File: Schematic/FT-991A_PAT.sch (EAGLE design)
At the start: 33 parts, among them Q1 PE4259, Q2 MC78L09ABDR2GOSCT, Q5 NCP553, Q7 J310, Q8 5086, X1 IF_IN, X2 SCP_OUT, X3 SDR_OUT

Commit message: Few more enhancements and impedance control
* Larger ground exposed ground pad near at the screw
* Changed pad for RF components to a rounded layout
* Enlarged the RF wire signal, in order to reduce the internal signal
  impedance
* Better component silk screen
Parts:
- C1, C10, C13, C6: device rcl:C-EUC0805 -> aarf:C-0805
- C11, C7: device rcl:C-EUC3216 -> aarf:C-1206
- D1: device diode:DIODE-SOD323-W -> aarf:D-SOD323
- L2, L3: device rcl-modified:L-EU -> aarf:FB-0805
- R10, R2, R3, R4, R5, R6, R7, R8, R9: device rcl:R-US_R3216 -> aarf:R-1206
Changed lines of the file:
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@@
 </classes>
 <parts>
-<part name="C6" library="rcl" library_urn="urn:adsk.eagle:library:334" deviceset="C-EU" device="C0805" package3d_urn="urn:adsk.eagle:package:23617/2" value="1000pF"/>
-<part name="R5" library="rcl" library_urn="urn:adsk.eagle:library:334" deviceset="R-US_" device="R3216" package3d_urn="urn:adsk.eagle:package:23557/2" value="100kΩ"/>
+<part name="C6" library="aarf" deviceset="C-0805" device="" value="1000pF"/>
+<part name="R5" library="aarf" deviceset="R-1206" device="" value="100kΩ"/>
 <part name="Q8" library="aarf" deviceset="2SC5086" device="" value="5086"/>
-<part name="R7" library="rcl" library_urn="urn:adsk.eagle:library:334" deviceset="R-US_" device="R3216" package3d_urn="urn:adsk.eagle:package:23557/2" value="1kΩ"/>
-<part name="C10" library="rcl" library_urn="urn:adsk.eagle:library:334" deviceset="C-EU" device="C0805" package3d_urn="urn:adsk.eagle:package:23617/2" value="1000pF"/>
+<part name="R7" library="aarf" deviceset="R-1206" device="" value="1kΩ"/>
+<part name="C10" library="aarf" deviceset="C-0805" device="" value="1000pF"/>
 <part name="GND11" library="supply1" deviceset="GNDA" device=""/>
-<part name="R6" library="rcl" library_urn="urn:adsk.eagle:library:334" deviceset="R-US_" device="R3216" package3d_urn="urn:adsk.eagle:package:23557/2" value="220Ω"/>
-<part name="C7" library="rcl" library_urn="urn:adsk.eagle:library:334" deviceset="C-EU" device="C3216" package3d_urn="urn:adsk.eagle:package:23628/2" value="0.1µF"/>
+<part name="R6" library="aarf" deviceset="R-1206" device="" value="220Ω"/>
+<part name="C7" library="aarf" deviceset="C-1206" device="" value="0.1µF"/>
 <part name="GND10" library="supply1" deviceset="GNDA" device=""/>
-<part name="C11" library="rcl" library_urn="urn:adsk.eagle:library:334" deviceset="C-EU" device="C3216" package3d_urn="urn:adsk.eagle:package:23628/2" value="0.1µF"/>
-<part name="R8" library="rcl" library_urn="urn:adsk.eagle:library:334" deviceset="R-US_" device="R3216" package3d_urn="urn:adsk.eagle:package:23557/2" value="10kΩ"/>
+<part name="C11" library="aarf" deviceset="C-1206" device="" value="0.1µF"/>
+<part name="R8" library="aarf" deviceset="R-1206" device="" value="10kΩ"/>
 <part name="GND19" library="supply1" deviceset="GNDA" device=""/>
 <part name="GND13" library="supply1" deviceset="GNDA" device=""/>
-<part name="R9" library="rcl" library_urn="urn:adsk.eagle:library:334" deviceset="R-US_" device="R3216" package3d_urn="urn:adsk.eagle:package:23557/2" value="1kΩ"/>
-<part name="R10" library="rcl" library_urn="urn:adsk.eagle:library:334" deviceset="R-US_" device="R3216" package3d_urn="urn:adsk.eagle:package:23557/2" value="220Ω"/>
+<part name="R9" library="aarf" deviceset="R-1206" device="" value="1kΩ"/>
+<part name="R10" library="aarf" deviceset="R-1206" device="" value="220Ω"/>
 <part name="GND16" library="supply1" deviceset="GNDA" device=""/>
 <part name="X3" library="adafruit" deviceset="ANTENNA_U.FL" device="" value="SDR_OUT"/>
@@
 <part name="X2" library="adafruit" deviceset="ANTENNA_U.FL" device="" value="SCP_OUT"/>
 <part name="GND4" library="supply1" deviceset="GNDA" device=""/>
-<part name="D1" library="diode" library_urn="urn:adsk.eagle:library:210" deviceset="DIODE-" device="SOD323-W" package3d_urn="urn:adsk.eagle:package:43418/1" value="1SS355VM"/>
+<part name="D1" library="aarf" deviceset="D-SOD323" device="" value="1SS355VM"/>
 <part name="PAD3" library="wirepad" library_urn="urn:adsk.eagle:library:412" deviceset="WIREPAD" device="SMD1,27-254" package3d_urn="urn:adsk.eagle:package:30839/1" value="TX9"/>
-<part name="R2" library="rcl" library_urn="urn:adsk.eagle:library:334" deviceset="R-US_" device="R3216" package3d_urn="urn:adsk.eagle:package:23557/2" value="1kΩ"/>
-<part name="C1" library="rcl" library_urn="urn:adsk.eagle:library:334" deviceset="C-EU" device="C0805" package3d_urn="urn:adsk.eagle:package:23617/2" value="1000pF"/>
+<part name="R2" library="aarf" deviceset="R-1206" device="" value="1kΩ"/>
+<part name="C1" library="aarf" deviceset="C-0805" device="" value="1000pF"/>
 <part name="13.8V" library="wirepad" library_urn="urn:adsk.eagle:library:412" deviceset="WIREPAD" device="SMD1,27-254" package3d_urn="urn:adsk.eagle:package:30839/1" value="13.8V"/>
-<part name="L2" library="rcl-modified" deviceset="L-EU" device="" value="BLM21"/>
+<part name="L2" library="aarf" deviceset="FB-0805" device="" value="BLM21"/>
 <part name="FRAME1" library="frames" library_urn="urn:adsk.eagle:library:229" deviceset="A3L-LOC" device="" value="F1"/>
 <part name="GND12" library="supply1" library_urn="urn:adsk.eagle:library:371" deviceset="GNDA" device=""/>
-<part name="R4" library="rcl" library_urn="urn:adsk.eagle:library:334" deviceset="R-US_" device="R3216" package3d_urn="urn:adsk.eagle:package:23557/2" value="5.6kΩ"/>
-<part name="R3" library="rcl" library_urn="urn:adsk.eagle:library:334" deviceset="R-US_" device="R3216" package3d_urn="urn:adsk.eagle:package:23557/2" value="10kΩ"/>
+<part name="R4" library="aarf" deviceset="R-1206" device="" value="5.6kΩ"/>
+<part name="R3" library="aarf" deviceset="R-1206" device="" value="10kΩ"/>
 <part name="GND2" library="supply1" library_urn="urn:adsk.eagle:library:371" deviceset="GNDA" device=""/>
-<part name="L3" library="rcl-modified" deviceset="L-EU" device="" value="BLM21"/>
-<part name="C13" library="rcl" library_urn="urn:adsk.eagle:library:334" deviceset="C-EU" device="C0805" package3d_urn="urn:adsk.eagle:package:23617/2" value="1000pF"/>
+<part name="L3" library="aarf" deviceset="FB-0805" device="" value="BLM21"/>
+<part name="C13" library="aarf" deviceset="C-0805" device="" value="1000pF"/>
 <part name="FRAME2" library="frames" library_urn="urn:adsk.eagle:library:229" deviceset="A3L-LOC" device=""/>
 <part name="GND5" library="supply1" library_urn="urn:adsk.eagle:library:371" deviceset="GNDA" device=""/>
@@
 packages will not be understood (or retained) with this version.
 </note>
-<note version="8.4" severity="warning">
-Since Version 8.4, EAGLE supports properties for SPICE simulation.
-Probes in schematics and SPICE mapping objects found in parts and library devices
-will not be understood with this version. Update EAGLE to the latest version
-for full support of SPICE simulation.
-</note>
 </compatibility>

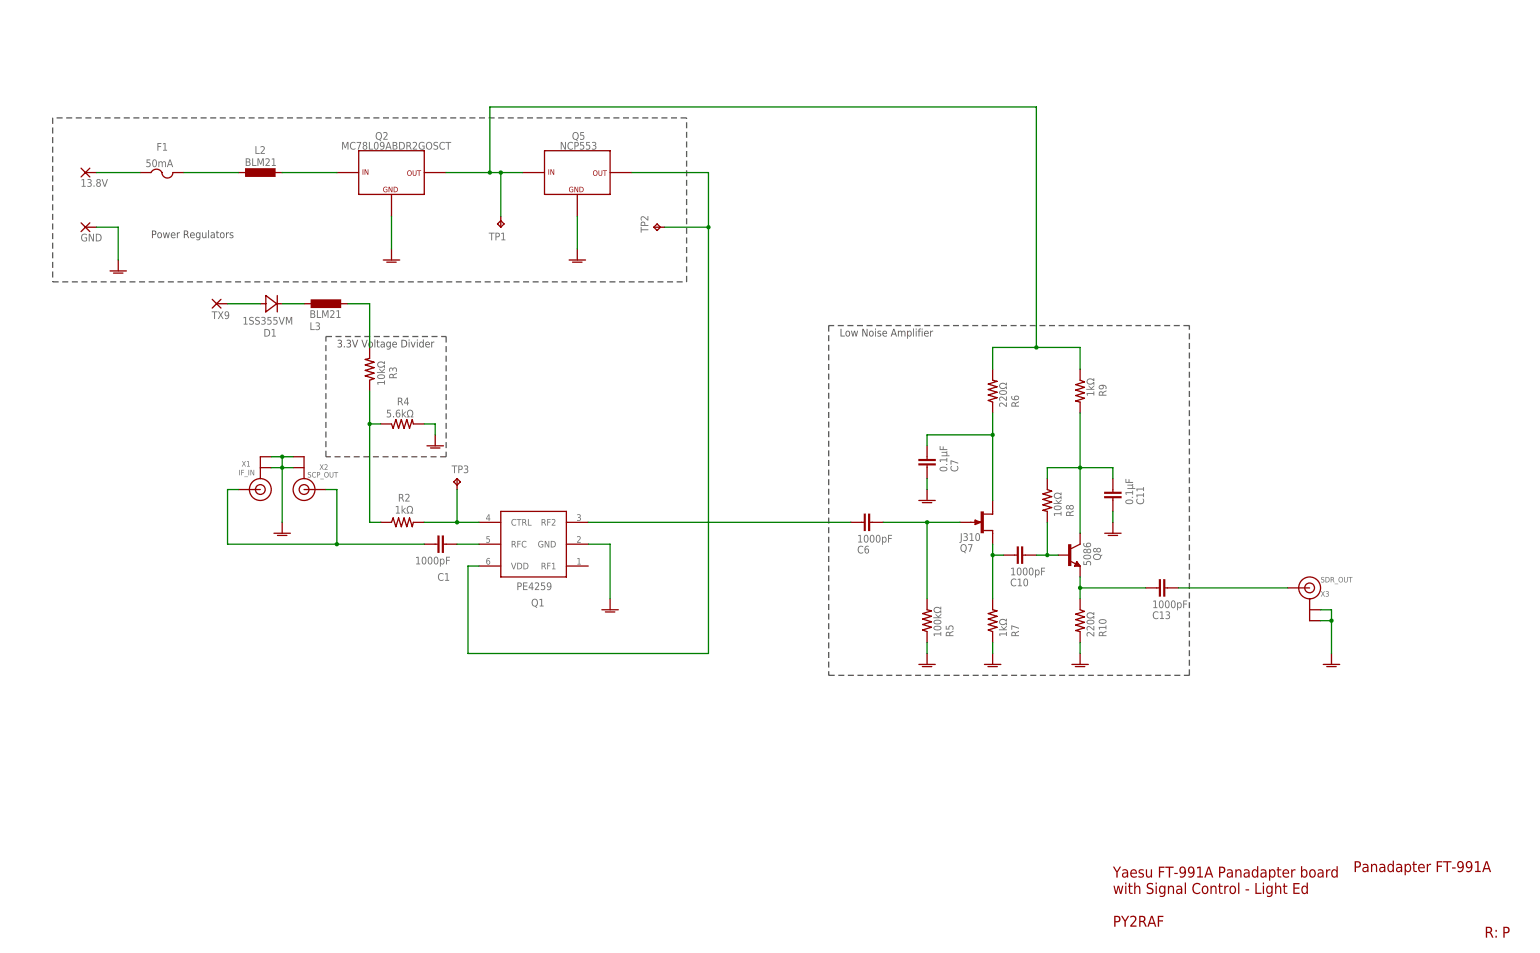
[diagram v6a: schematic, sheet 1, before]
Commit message: Rev. Q: Rew improvements
* Moved TX9 signal treatment compoments from board lid to larger board
* Changed fuse silk screen
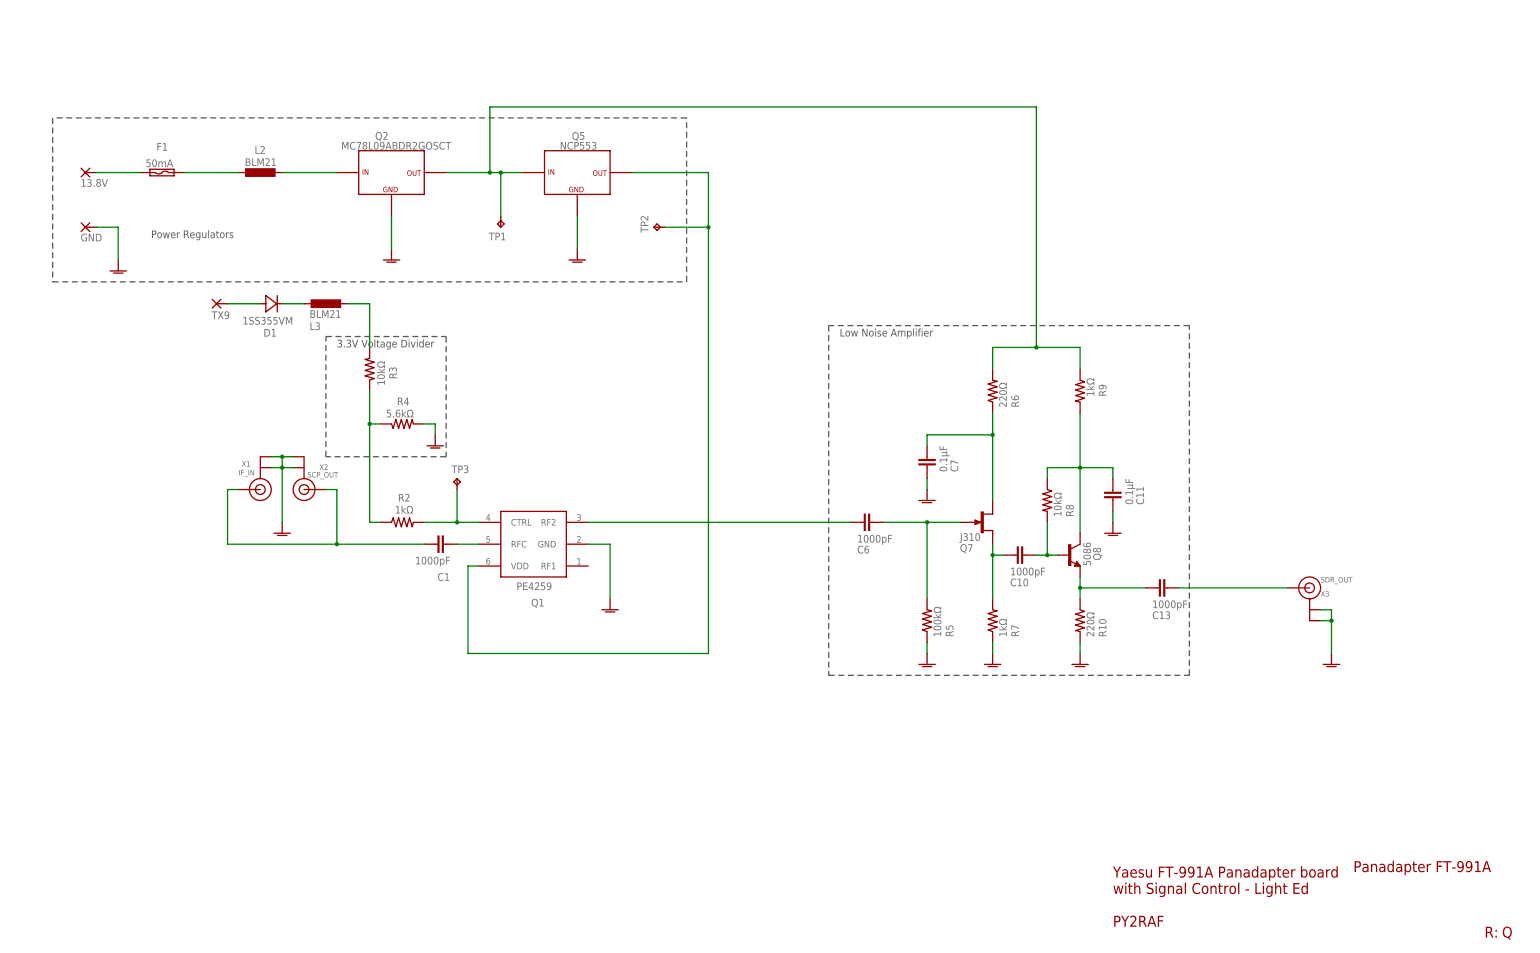
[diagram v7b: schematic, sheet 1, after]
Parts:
- F1: device adafruit:PTCFUSE-1206 -> aarf:FUSE-1206
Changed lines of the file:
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@@
 <attribute name="PROJECT_INFO" value="Yaesu FT-991A Panadapter with Signal Control"/>
 <attribute name="PROJECT_NAME" value="FT-991A PAT &amp; SDR"/>
-<attribute name="REVISION_ID" value="P"/>
+<attribute name="REVISION_ID" value="Q"/>
 </attributes>
 <variantdefs>
@@
 <part name="GND5" library="supply1" library_urn="urn:adsk.eagle:library:371" deviceset="GNDA" device=""/>
 <part name="Q5" library="aarf" deviceset="NCP553" device=""/>
-<part name="F1" library="adafruit" deviceset="PTCFUSE" device="-1206" value="50mA"/>
+<part name="F1" library="aarf" deviceset="FUSE-1206" device="" value="50mA"/>
 <part name="Q2" library="aarf" deviceset="MC78L" device="" technology="09ABDR2GOSCT"/>
 <part name="Q1" library="aarf" deviceset="PE4259" device="" value="PE4259"/>
@@
 <attribute name="NAME" x="163.83" y="190.5" size="1.778" layer="95"/>
 </instance>
-<instance part="F1" gate="G$1" x="68.58" y="180.34" smashed="yes">
+<instance part="F1" gate="G$1" x="68.58" y="182.88" smashed="yes">
 <attribute name="VALUE" x="64.77" y="184.15" size="1.778" layer="96"/>
 <attribute name="NAME" x="67.31" y="187.96" size="1.778" layer="95"/>

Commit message: Starring: Revision R
Check CHANGELOG.md file.
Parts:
- removed C6: 1000pF, aarf:C-0805
- removed R6: 220Ω, aarf:R-1206
- removed R9: 1kΩ, aarf:R-1206
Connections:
- removed net 9V5086: C11.1, Q8.C, R8.1, R9.2
- removed net 9VJ310: C7.1, Q7.S, R6.1
- removed net N$6: C6.2, Q7.G, R5.2
- net 3V: now also C11.1, Q8.C, R8.1
- net 9V: now also C7.1, Q7.S; no longer R6.2, R9.1
- net IFIN: now also Q7.G, R5.2; no longer C6.1
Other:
- note added: "J310 Preamp"
- note added: "RF Switch 2SC5086 LNA"
- note removed: "Amplifiers"
- note removed: "Switch"
